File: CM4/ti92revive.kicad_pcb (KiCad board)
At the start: 2 copper layers, 205 x 116.7 mm, 178 parts, among them J1 USB_B, J2 Bat0, J3 Bat1, J4 USB_A, J5 USB_A, Q1 EMH3, U1 Compute_Module_4_Connectors, U10 4inch_RPi_LCD_(C), U2 NCP114ASN330T1G, U3 BQ25887RGET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

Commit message: Keyboard close to done
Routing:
- net col9: track 0.00 -> 288.7 mm, vias 0 -> 14
- net row2: track 69.6 -> 173.4 mm, vias 3 -> 12
- net row6: track 198.8 -> 238.9 mm, vias 10 -> 14
- net col5: track 344.0 -> 356.6 mm
- net col6: track 339.0 -> 343.7 mm
- net col3: track 382.5 -> 386.7 mm
- net col8: track 361.5 -> 363.2 mm
- net col7: track 423.1 -> 424.6 mm
- net row4: track 344.0 -> 343.2 mm

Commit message: Keyboard Done <3
adding a layer for signals that need to be *Clean*
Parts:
- moved R16 58.7 mm to (130.0, 72.2), turned to 0 degrees
- moved R17 51.5 mm to (130.0, 67.8), turned to 0 degrees
- moved C17 15.0 mm to (85.5, 61.5), turned to 0 degrees
- moved C16 12.5 mm to (85.5, 67.9), turned to 0 degrees
- moved U8 12.2 mm to (85.5, 64.7), turned to 0 degrees
- moved C12 5.49 mm to (85.6, 53.0)
- moved C13 5.49 mm to (85.6, 59.0)
- moved U2 5.49 mm to (85.8, 56.0)
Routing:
- net col0: track 131.9 -> 489.1 mm, vias 2 -> 12
- net row0: track 151.4 -> 283.3 mm, vias 1 -> 4
- net Net-(R16-Pad2): track 0.00 -> 14.5 mm
- net Net-(JP3-Pad2): track 19.9 -> 12.6 mm
- net Earth_Clean: track 69.8 -> 76.7 mm, vias 2 -> 3
- net col2: track 346.2 -> 351.6 mm
- net Net-(JP2-Pad1): track 18.2 -> 13.4 mm, vias 2 -> 0
- net Net-(TP21-Pad1): track 0.00 -> 4.71 mm
- net Net-(TP20-Pad1): track 0.00 -> 4.00 mm
- net +5: track 48.9 -> 52.7 mm, vias 4 -> 5
- net col8: track 363.2 -> 359.5 mm
- net col6: track 343.7 -> 346.2 mm
- net col7: track 424.6 -> 422.9 mm

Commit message: boys we got 2 more layers to play with now >.<
(oh god this is so much stuff hehehehehehe.... ima go mad with power)
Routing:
- net Earth_Clean: track 76.7 -> 164.1 mm, vias 3 -> 7
- net +5: track 52.7 -> 38.7 mm, vias 5 -> 3
- net col0: track 489.1 -> 487.9 mm
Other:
- copper layers 2 -> 4

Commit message: routing fun!!
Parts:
- moved J2 206.1 mm to (69.4, 57.2)
- moved TH1 205.5 mm to (66.5, 68.0)
- moved JP4 80.2 mm to (247.0, 68.8), turned to 90 degrees
- moved Q1 55.0 mm to (95.0, 79.8)
- moved R15 47.7 mm to (88.4, 78.6), turned to -90 degrees
- moved J3 41.9 mm to (247.2, 75.6)
- moved JP1 41.6 mm to (113.9, 89.4)
- moved R12 41.6 mm to (107.3, 94.8)
- moved R13 41.6 mm to (107.3, 100.0)
- moved U5 41.6 mm to (119.8, 93.6)
- moved U6 33.9 mm to (97.6, 67.4), turned to 180 degrees
- moved D84 24.5 mm to (101.0, 77.1), turned to 0 degrees
- moved D83 19.6 mm to (94.6, 77.1), turned to 180 degrees
- moved U10 11.1 mm to (157.4, 93.7)
- moved J1 2.60 mm to (219.4, 35.2)
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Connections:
- J1 pad 6: (no net) -> Earth_Clean
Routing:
- net +5: track 38.7 -> 348.5 mm, vias 3 -> 10
- net Earth_Clean: track 164.1 -> 454.5 mm, vias 7 -> 11
- net batCell+: track 5.20 -> 266.1 mm, vias 0 -> 1
- net 5vRegulator: track 4.99 -> 108.4 mm, vias 0 -> 2
- net Net-(C4-Pad2): track 4.41 -> 105.5 mm
- net Net-(U5-Pad5): track 0.00 -> 96.1 mm, vias 0 -> 2
- net BAT+: track 0.00 -> 62.8 mm, vias 0 -> 4
- net Net-(R15-Pad1): track 0.00 -> 28.7 mm, vias 0 -> 2
- net Net-(C15-Pad1): track 0.00 -> 19.1 mm
- net Net-(C14-Pad1): track 0.00 -> 14.0 mm
- net Net-(D84-Pad2): track 0.00 -> 13.1 mm, vias 0 -> 2
- net Net-(D83-Pad2): track 0.00 -> 7.51 mm
- net Net-(D81-Pad2): track 0.00 -> 6.55 mm, vias 0 -> 1
- net Net-(D4-Pad1): track 0.00 -> 2.92 mm, vias 0 -> 1
- net Net-(D2-Pad1): track 0.00 -> 2.85 mm, vias 0 -> 1
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
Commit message: 100 things left to rout
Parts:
- added TP25: TestPoint, TestPoint:TestPoint_Pad_D1.0mm, F.Cu at (122.2, 93.6)
- moved R12 153.4 mm to (252.2, 44.2)
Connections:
- U5 pad 1: unconnected-(U5-Pad1) -> Net-(U5-Pad1)
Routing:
- net Net-(D82-Pad2): track 0.00 -> 195.4 mm, vias 0 -> 4
- net +1.8: track 3.37 -> 133.2 mm, vias 1 -> 3
- net BAT+: track 62.8 -> 188.7 mm, vias 4 -> 5
- net +3.3: track 0.00 -> 95.7 mm, vias 0 -> 3
- net piWatchDogPin: track 0.00 -> 86.0 mm, vias 0 -> 2
- net Net-(R12-Pad2): track 0.00 -> 66.2 mm, vias 0 -> 2
- net SetPowerOFF: track 0.00 -> 30.8 mm, vias 0 -> 1
- net SetPowerON: track 0.00 -> 27.4 mm
- net Net-(D1-Pad2): track 0.00 -> 7.54 mm, vias 0 -> 1
- net +5: track 348.5 -> 355.5 mm
- net Net-(R13-Pad1): track 0.00 -> 4.85 mm
- net Earth_Clean: track 454.5 -> 457.2 mm
- net Net-(U5-Pad1): track 0.00 -> 2.46 mm
- net Net-(R1-Pad2): track 18.1 -> 19.9 mm
- net col2: track 351.6 -> 350.9 mm
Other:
- board text added: "PB5"

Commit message: 75 left to go
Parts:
- moved R19 86.3 mm to (226.2, 66.4), turned to 0 degrees
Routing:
- net Net-(R18-Pad1): track 0.00 -> 227.0 mm, vias 0 -> 2
- net Net-(R20-Pad1): track 0.00 -> 218.7 mm, vias 0 -> 2
- net Net-(D81-Pad1): track 0.00 -> 156.8 mm, vias 0 -> 4
- net CCVref: track 10.5 -> 153.1 mm, vias 0 -> 2
- net +1: track 5.54 -> 98.2 mm, vias 0 -> 4
- net /USB and Keyboard connections/KEYBOARD_USB_DN: track 0.00 -> 89.7 mm, vias 0 -> 2
- net /USB and Keyboard connections/KEYBOARD_USB_DP: track 0.00 -> 83.8 mm, vias 0 -> 2
- net +3.3 High Current: track 2.23 -> 83.0 mm, vias 0 -> 7
- net Net-(JP4-Pad2): track 0.00 -> 54.5 mm, vias 0 -> 2
- net Net-(J4-Pad2): track 0.00 -> 30.2 mm, vias 0 -> 2
- net Net-(J4-Pad3): track 0.00 -> 28.5 mm, vias 0 -> 2
- net Net-(J5-Pad3): track 0.00 -> 25.0 mm, vias 0 -> 1
- net Net-(J5-Pad2): track 0.00 -> 23.8 mm, vias 0 -> 1
- net Net-(JP4-Pad1): track 0.00 -> 20.3 mm
- net col6: track 346.2 -> 344.6 mm
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
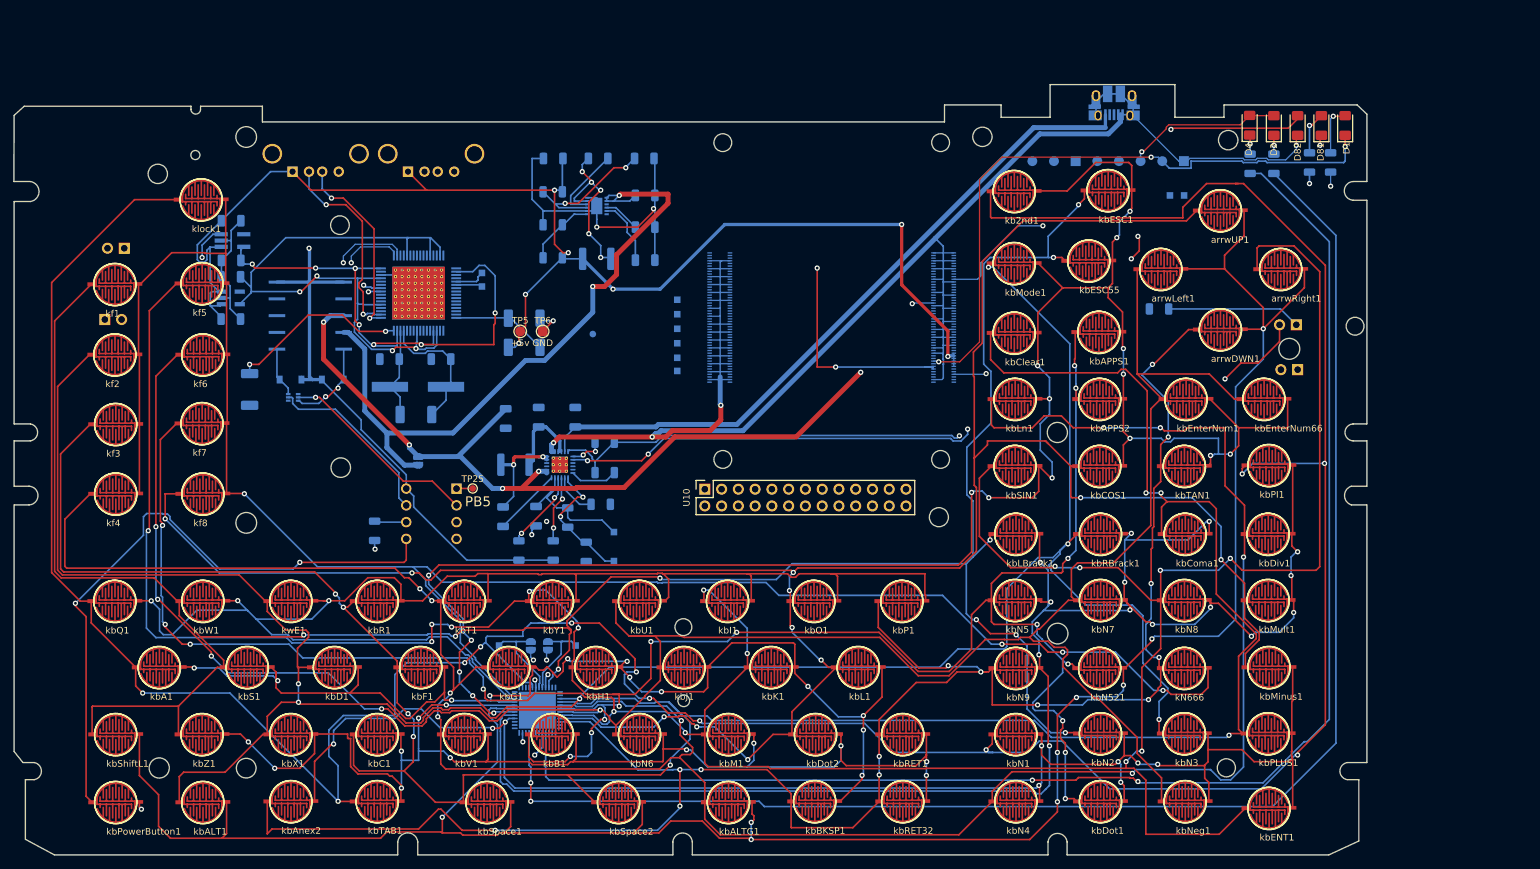
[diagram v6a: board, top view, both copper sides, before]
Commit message: Everything is routed
Just waiting on display to finsh routing that, then its time to get some pcbs on the way and cross my fingers that i dont cook a cm4 >.<
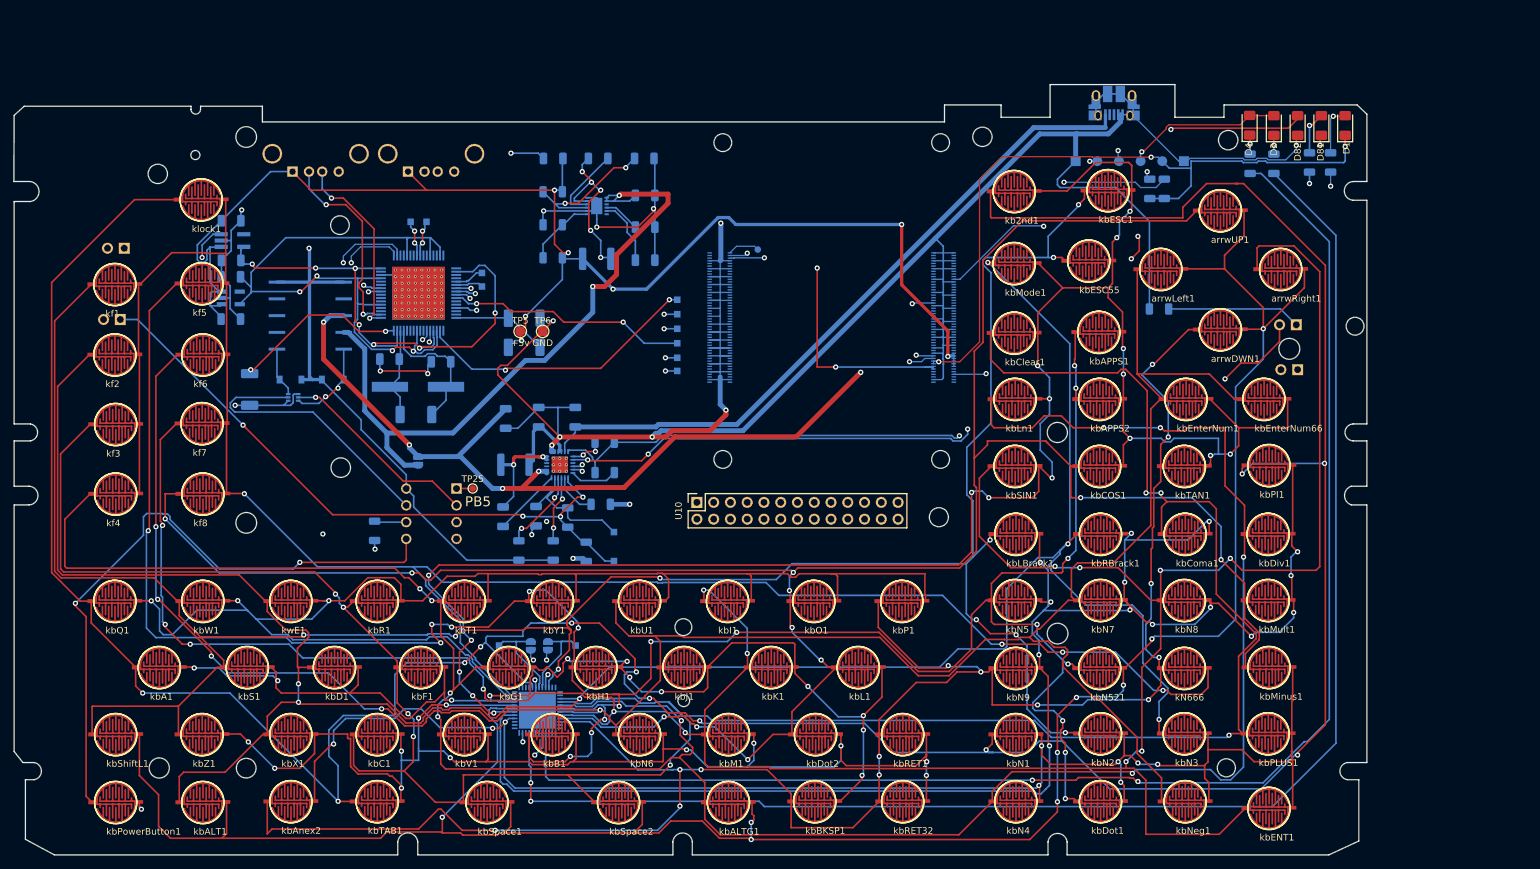
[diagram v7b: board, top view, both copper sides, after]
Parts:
- removed TP8: 14, TestPoint:TestPoint_Pad_D1.5mm
- removed TP9: 15, TestPoint:TestPoint_Pad_D1.5mm
- added R21: R_US, Resistor_SMD:R_1206_3216Metric, B.Cu at (227.0, 48.2)
- added R22: R_US, Resistor_SMD:R_1206_3216Metric, B.Cu at (224.8, 48.2)
- moved TP14 115.1 mm to (112.8, 53.2)
- moved TP15 114.9 mm to (115.2, 53.2)
- moved TP12 28.1 mm to (165.4, 57.4)
- moved TH1 2.34 mm to (68.8, 68.0), turned to 90 degrees
- moved U10 2.33 mm to (156.2, 95.7)
- moved C15 0.40 mm to (117.4, 74.4)
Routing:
- net Earth_Clean: track 457.2 -> 934.7 mm, vias 11 -> 22
- net SDA: track 0.00 -> 129.3 mm, vias 0 -> 4
- net SCL: track 0.00 -> 115.3 mm, vias 0 -> 4
- net Net-(R1-Pad2): track 19.9 -> 99.0 mm, vias 2 -> 4
- net USB_HOST_N: track 0.00 -> 76.0 mm, vias 0 -> 2
- net USB_HOST_P: track 0.00 -> 72.9 mm, vias 0 -> 2
- net Net-(TP13-Pad1): track 0.00 -> 43.4 mm, vias 0 -> 2
- net Net-(TP19-Pad1): track 0.00 -> 37.9 mm, vias 0 -> 2
- net Net-(TP17-Pad1): track 0.00 -> 37.7 mm, vias 0 -> 2
- net Net-(TP18-Pad1): track 0.00 -> 36.3 mm, vias 0 -> 2
- net Net-(TP16-Pad1): track 0.00 -> 35.8 mm, vias 0 -> 2
- net Net-(TP22-Pad1): track 0.00 -> 35.1 mm, vias 0 -> 2
- net SetPowerON: track 27.4 -> 42.6 mm
- net +3.3: track 95.7 -> 105.9 mm
- net Net-(TP14-Pad1): track 0.00 -> 5.49 mm, vias 0 -> 2
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
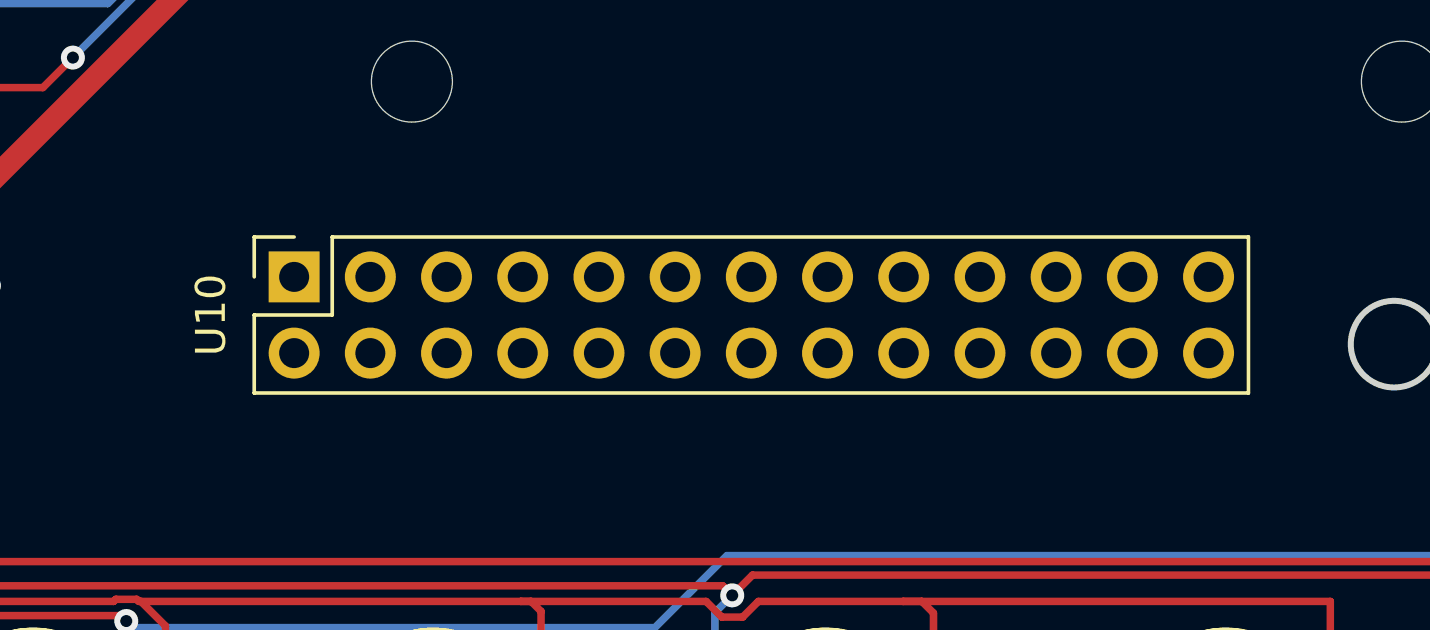
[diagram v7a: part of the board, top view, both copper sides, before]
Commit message: Bigone here we go
Whats gonna happon is im gonna get a 4 inch hdmi display and desolder the hdmi connector and add it to a ribbion cable and then add a connector to the pcb for hdmi to interface with that
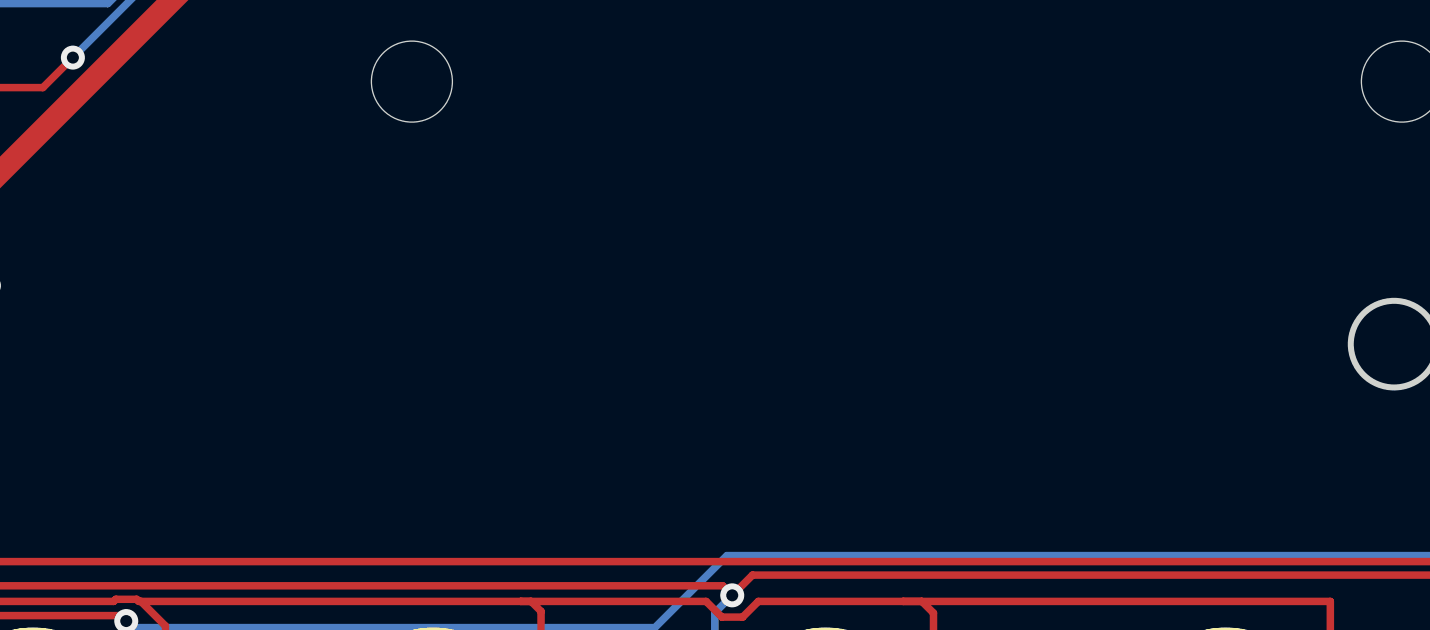
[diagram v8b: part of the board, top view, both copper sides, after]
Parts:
- removed U10: 4inch_RPi_LCD_(C), Connector_PinSocket_2.54mm:PinSocket_2x13_P2.54mm_Vertical
